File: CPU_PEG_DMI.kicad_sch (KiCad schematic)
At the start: 1 part

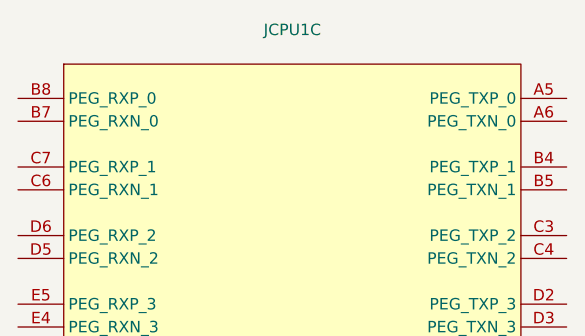
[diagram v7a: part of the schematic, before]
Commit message: Added first PCH symbol and footprint
THANKS @mothenjoyer69 so much for extracting and converting the PCH footprint from a laptop boardview ❤️
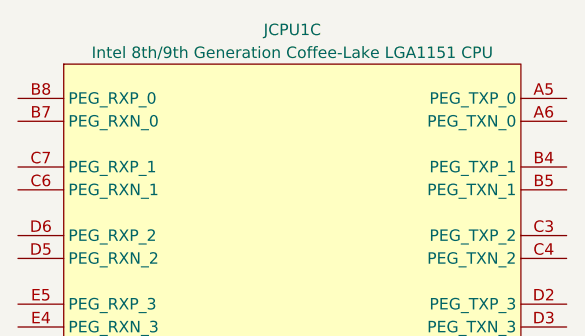
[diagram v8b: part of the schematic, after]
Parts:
- JCPU1: value ~ -> Intel 8th/9th Generation Coffee-Lake LGA1151 CPU
